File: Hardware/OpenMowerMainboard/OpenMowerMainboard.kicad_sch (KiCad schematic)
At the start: 9 parts, among them U1 LM2596S_MODULE

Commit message: wip schematic
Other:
- note added: "TODO pinouts pruefen stecker pinout pruefen regensensor led platine connector ladestrom sicherungen original stecker recherchieren add testpads"
- note removed: "TODO stecker checken regensensor led platine connector lade und systemspannung lade und entladestrom pi <--> pico programmer? IMU? sound? TVS schutzdioden sicherungen original stecker recherchieren many testpads speaker connector"
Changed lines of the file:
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@@
     (effects (font (size 1.27 1.27)) (justify left bottom))
   )
-  (text "TODO\nstecker checken\nregensensor\nled platine connector\nlade und systemspannung\nlade und entladestrom\npi <--> pico programmer?\nIMU?\nsound?\nTVS schutzdioden\nsicherungen\noriginal stecker recherchieren\nmany testpads\nspeaker connector"
+  (text "TODO\npinouts pruefen\nstecker pinout pruefen\nregensensor\nled platine connector\nladestrom\nsicherungen\noriginal stecker recherchieren\nadd testpads"
     (at 288.29 66.675 0)
     (effects (font (size 1.27 1.27)) (justify left bottom))
@@
       (reference "D3") (unit 1) (value "D_Schottky") (footprint "")
     )
+    (path "/a66eb396-0410-43f5-a37d-ef2abb980a3a/4ebdc7ab-25b0-4467-9229-087b84fdf66f"
+      (reference "D4") (unit 1) (value "D_TVS") (footprint "Diode_SMD:D_SMB")
+    )
+    (path "/a66eb396-0410-43f5-a37d-ef2abb980a3a/55b8a13b-6894-4208-a000-86cbaab261aa"
+      (reference "D5") (unit 1) (value "D_TVS") (footprint "Diode_SMD:D_SMB")
+    )
+    (path "/a66eb396-0410-43f5-a37d-ef2abb980a3a/37a9969b-e03a-4c0a-94f9-c1bfb2bcb429"
+      (reference "D6") (unit 1) (value "D_TVS") (footprint "Diode_SMD:D_SMB")
+    )
+    (path "/a66eb396-0410-43f5-a37d-ef2abb980a3a/56203402-79b1-40a1-97ad-4c42312e0916"
+      (reference "D7") (unit 1) (value "D_TVS") (footprint "Diode_SMD:D_SMB")
+    )
+    (path "/a66eb396-0410-43f5-a37d-ef2abb980a3a/dcbf07c1-fd83-46b4-9cb8-68d7fd77aad4"
+      (reference "D8") (unit 1) (value "D_TVS") (footprint "Diode_SMD:D_SMB")
+    )
+    (path "/a66eb396-0410-43f5-a37d-ef2abb980a3a/8d636e49-195d-4662-8b69-230d986a3b72"
+      (reference "D9") (unit 1) (value "D_TVS") (footprint "Diode_SMD:D_SMB")
+    )
+    (path "/a66eb396-0410-43f5-a37d-ef2abb980a3a/2bebeb4d-3b78-44b1-9d84-649cd389bb68"
+      (reference "D10") (unit 1) (value "D_TVS") (footprint "Diode_SMD:D_SMB")
+    )
+    (path "/a66eb396-0410-43f5-a37d-ef2abb980a3a/20b8b1d3-3d67-4311-99ca-ce5363c0cad0"
+      (reference "D11") (unit 1) (value "D_TVS") (footprint "Diode_SMD:D_SMB")
+    )
+    (path "/a66eb396-0410-43f5-a37d-ef2abb980a3a/a6025457-ad02-406e-ac1d-03834a754964"
+      (reference "D12") (unit 1) (value "D_TVS") (footprint "Diode_SMD:D_SMB")
+    )
+    (path "/00000000-0000-0000-0000-000061040c60/520089b0-4442-4713-ae1b-87d63d51b467"
+      (reference "F1") (unit 1) (value "Fuse") (footprint "MyModules:Fuseholder5x20_horiz_open_inline_Type-I")
+    )
+    (path "/00000000-0000-0000-0000-000061040c60/b9168f77-b5a5-4161-8a9b-951a2e8475d3"
+      (reference "F2") (unit 1) (value "Fuse") (footprint "MyModules:Fuseholder5x20_horiz_open_inline_Type-I")
+    )
+    (path "/00000000-0000-0000-0000-000061040c60/89a9550d-36a5-40f8-a465-c83bb62d834f"
+      (reference "F3") (unit 1) (value "Fuse") (footprint "MyModules:Fuseholder5x20_horiz_open_inline_Type-I")
+    )
+    (path "/00000000-0000-0000-0000-000061040c60/58391851-bdb9-4e0a-bc80-50f6a07fc993"
+      (reference "F4") (unit 1) (value "Fuse") (footprint "MyModules:Fuseholder5x20_horiz_open_inline_Type-I")
+    )
     (path "/00000000-0000-0000-0000-000060ffea54"
       (reference "H1") (unit 1) (value "MountingHole_Pad") (footprint "MountingHole:MountingHole_5mm_Pad")
@@
       (reference "J10") (unit 1) (value "Conn_01x05") (footprint "Connector_JST:JST_PH_B5B-PH-K_1x05_P2.00mm_Vertical")
     )
-    (path "/df7e4e30-b8d5-4f4b-a24f-39298e982d26/00000000-0000-0000-0000-00006130130c"
-      (reference "J11") (unit 1) (value "Conn_01x10_Female") (footprint "Connector_PinHeader_2.54mm:PinHeader_1x10_P2.54mm_Vertical")
-    )
     (path "/00000000-0000-0000-0000-000061040c60/b1812e93-6d07-48bc-8440-4307c7b13cf3"
       (reference "J11") (unit 1) (value "Conn_01x03_Male") (footprint "Connector_JST:JST_XH_B3B-XH-A_1x03_P2.50mm_Vertical")
@@
       (reference "J19") (unit 1) (value "Conn_01x04") (footprint "Connector_JST:JST_XH_B4B-XH-A_1x04_P2.50mm_Vertical")
     )
+    (path "/df7e4e30-b8d5-4f4b-a24f-39298e982d26/00000000-0000-0000-0000-00006130130c"
+      (reference "J20") (unit 1) (value "Conn_01x10_Female") (footprint "Connector_PinHeader_2.54mm:PinHeader_1x10_P2.54mm_Vertical")
+    )
     (path "/00000000-0000-0000-0000-00006109dce5/06715042-9807-4840-bc8e-1cf593cdbcdf"
       (reference "JP1") (unit 1) (value "SolderJumper_3_Bridged12") (footprint "")
@@
       (reference "R50") (unit 1) (value "10k") (footprint "Resistor_THT:R_Axial_DIN0309_L9.0mm_D3.2mm_P12.70mm_Horizontal")
     )
+    (path "/00000000-0000-0000-0000-000061040c60/f11b3e3a-7b08-49d8-b4b1-92030ffe70c2"
+      (reference "R51") (unit 1) (value "R") (footprint "Resistor_SMD:R_Shunt_Vishay_WSK2512_6332Metric_T2.66mm")
+    )
     (path "/989a400d-9ce2-403e-a19e-ad0a758fe27c/b948dd43-413f-4002-adce-e082c45a5179"
       (reference "R53") (unit 1) (value "1k5") (footprint "Resistor_THT:R_Axial_DIN0309_L9.0mm_D3.2mm_P12.70mm_Horizontal")
@@
       (reference "R57") (unit 1) (value "27k") (footprint "Resistor_THT:R_Axial_DIN0309_L9.0mm_D3.2mm_P12.70mm_Horizontal")
     )
-    (path "/00000000-0000-0000-0000-000061040c60/f11b3e3a-7b08-49d8-b4b1-92030ffe70c2"
-      (reference "R?") (unit 1) (value "R") (footprint "Resistor_SMD:R_Shunt_Vishay_WSK2512_6332Metric_T2.66mm")
-    )
     (path "/989a400d-9ce2-403e-a19e-ad0a758fe27c/88528529-64b3-4d79-b2db-e04c4b468443"

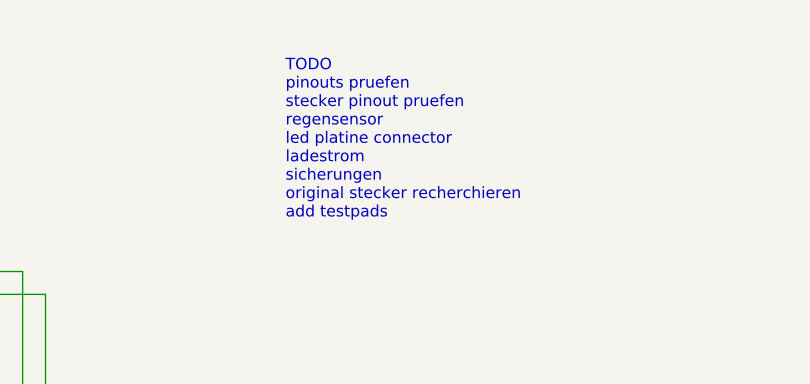
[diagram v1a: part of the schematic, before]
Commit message: removed unused io expander
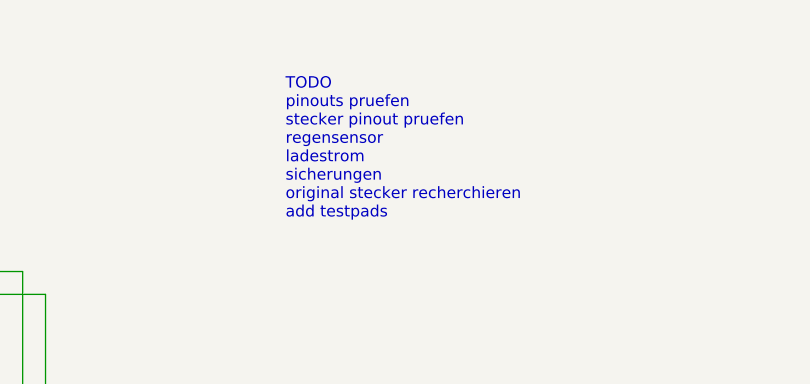
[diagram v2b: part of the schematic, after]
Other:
- note added: "TODO pinouts pruefen stecker pinout pruefen regensensor ladestrom sicherungen original stecker recherchieren add testpads"
- note removed: "TODO pinouts pruefen stecker pinout pruefen regensensor led platine connector ladestrom sicherungen original stecker recherchieren add testpads"
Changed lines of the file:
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@@
     (effects (font (size 1.27 1.27)) (justify left bottom))
   )
-  (text "TODO\npinouts pruefen\nstecker pinout pruefen\nregensensor\nled platine connector\nladestrom\nsicherungen\noriginal stecker recherchieren\nadd testpads"
+  (text "TODO\npinouts pruefen\nstecker pinout pruefen\nregensensor\nladestrom\nsicherungen\noriginal stecker recherchieren\nadd testpads"
     (at 288.29 66.675 0)
     (effects (font (size 1.27 1.27)) (justify left bottom))

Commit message: added footprints to schematic
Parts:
- R40, R41, R42, R43: footprint Resistor_SMD:R_0805_2012Metric -> Resistor_SMD:R_0805_2012Metric_Pad1.20x1.40mm_HandSolder
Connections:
- no-connect marks 1 -> 0
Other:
- sheet RobotConnectors ports: added none; removed V_BATT_ALWAYS_ON
- note removed: "Power In"

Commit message: routing mostly done
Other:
- sheet RobotConnectors ports: added CHARGE_SHUNT_MINUS, CHARGE_SHUNT_PLUS, SPEAKER_MINUS, SPEAKER_PLUS; removed CHARGE_SHUNT+, CHARGE_SHUNT-, SPEAKER+, SPEAKER-
- sheet opamps ports: added SHUNT_CHARGE_CURRENT_MINUS, SHUNT_CHARGE_CURRENT_PLUS; removed SHUNT_CHARGE_CURRENT+, SHUNT_CHARGE_CURRENT-
- sheet sound ports: added SPEAKER_MINUS, SPEAKER_PLUS; removed SPEAKER+, SPEAKER-
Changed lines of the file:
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@@
-      (effects (font (size 1.27 1.27)) (justify right))
-    )
-    (pin "SPEAKER-" input (at 68.58 233.68 0)
-      (effects (font (size 1.27 1.27)) (justify right))
-    )
-    (pin "SPEAKER+" input (at 68.58 231.14 0)
       (effects (font (size 1.27 1.27)) (justify right))
     )
@@
       (effects (font (size 1.27 1.27)) (justify right))
     )
-    (pin "CHARGE_SHUNT+" output (at 68.58 243.205 0)
+    (pin "SPEAKER_PLUS" input (at 68.58 231.14 0)
       (effects (font (size 1.27 1.27)) (justify right))
     )
-    (pin "CHARGE_SHUNT-" output (at 68.58 245.745 0)
+    (pin "SPEAKER_MINUS" input (at 68.58 233.68 0)
+      (effects (font (size 1.27 1.27)) (justify right))
+    )
+    (pin "CHARGE_SHUNT_PLUS" output (at 68.58 243.205 0)
+      (effects (font (size 1.27 1.27)) (justify right))
+    )
+    (pin "CHARGE_SHUNT_MINUS" output (at 68.58 245.745 0)
       (effects (font (size 1.27 1.27)) (justify right))
     )
@@
       (effects (font (size 1.27 1.27)) (justify left))
     )
-    (pin "SPEAKER-" output (at 223.52 233.68 180)
+    (pin "RESET" input (at 223.52 227.33 180)
       (effects (font (size 1.27 1.27)) (justify left))
     )
-    (pin "SPEAKER+" output (at 223.52 231.14 180)
+    (pin "SPEAKER_PLUS" output (at 223.52 231.14 180)
       (effects (font (size 1.27 1.27)) (justify left))
     )
-    (pin "RESET" input (at 223.52 227.33 180)
+    (pin "SPEAKER_MINUS" output (at 223.52 233.68 180)
       (effects (font (size 1.27 1.27)) (justify left))
     )
@@
       (effects (font (size 1.27 1.27)) (justify right))
     )
-    (pin "SHUNT_CHARGE_CURRENT+" input (at 203.2 243.205 180)
+    (pin "SHUNT_CHARGE_CURRENT_PLUS" input (at 203.2 243.205 180)
       (effects (font (size 1.27 1.27)) (justify left))
     )
-    (pin "SHUNT_CHARGE_CURRENT-" input (at 203.2 245.745 180)
+    (pin "SHUNT_CHARGE_CURRENT_MINUS" input (at 203.2 245.745 180)
       (effects (font (size 1.27 1.27)) (justify left))
     )

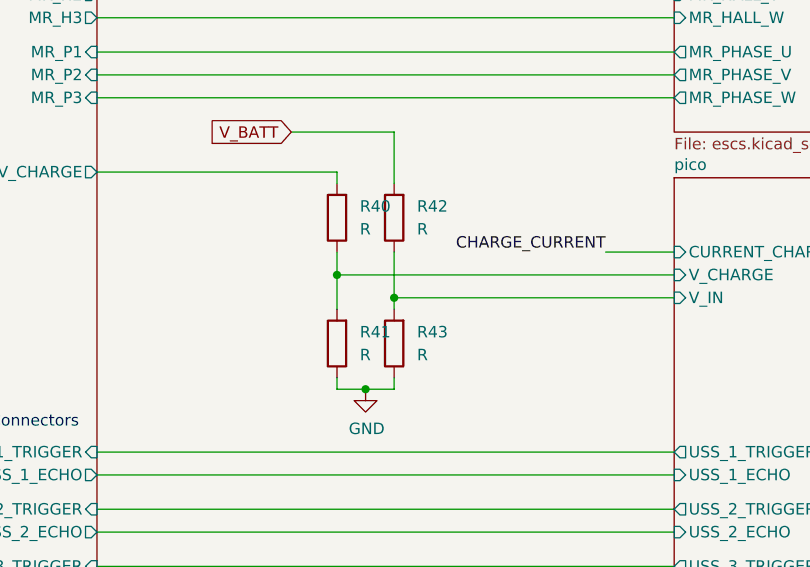
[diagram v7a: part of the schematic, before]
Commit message: update Resistance Values
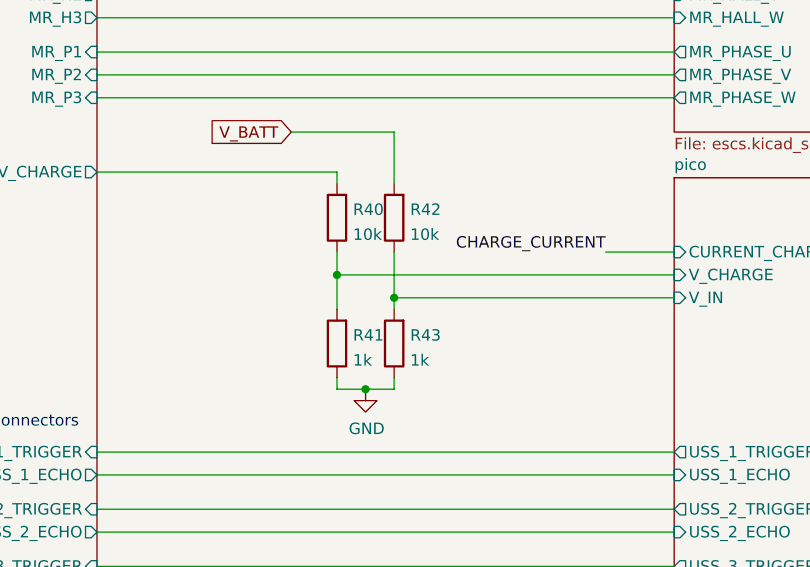
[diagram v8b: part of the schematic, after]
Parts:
- R40, R42: value R -> 10k
- R41, R43: value R -> 1k
